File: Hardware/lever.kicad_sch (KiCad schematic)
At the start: 11 parts

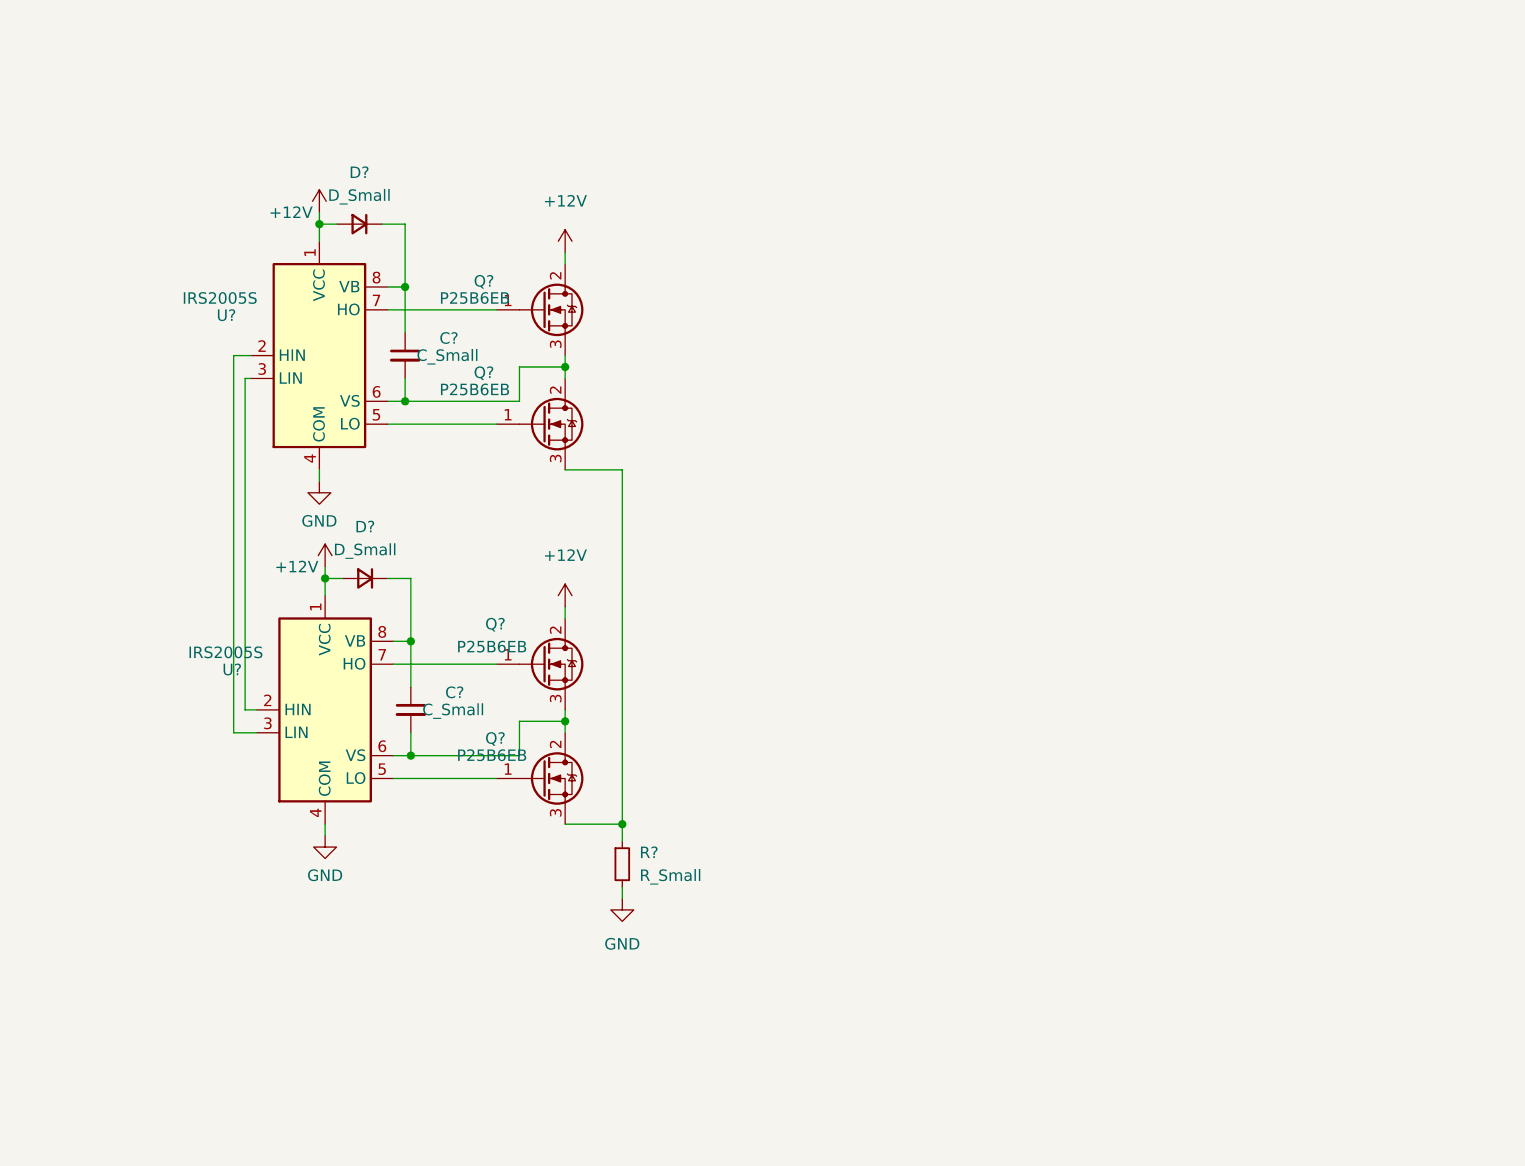
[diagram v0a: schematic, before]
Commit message: Polished coil driver. H bridge driver needs more work.
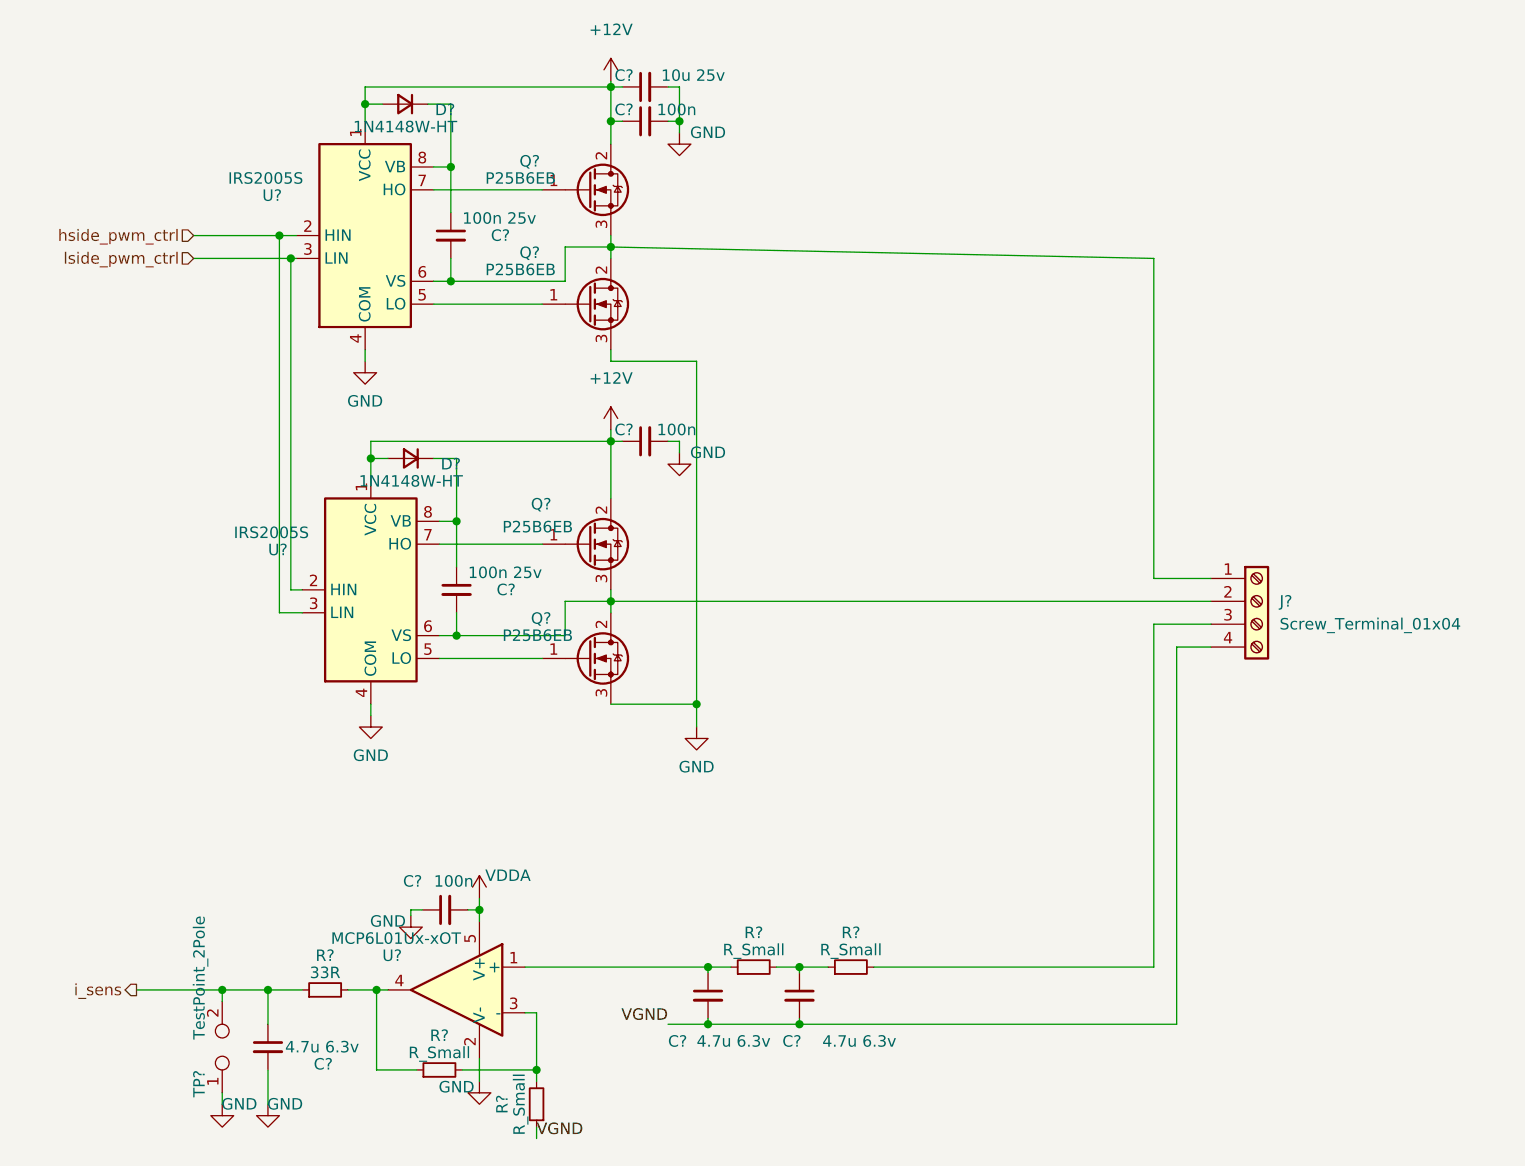
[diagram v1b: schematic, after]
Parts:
- removed C? (x2): C_Small, symbol Device:C_Small
- removed D? (x2): D_Small, symbol Device:D_Small
- removed R?: R_Small, symbol Device:R_Small
- added C? (x3): 100n, Capacitor_SMD:C_0603_1608Metric_Pad1.08x0.95mm_HandSolder, symbol Device:C_Small
- added C? (x3): 4.7u 6.3v, Capacitor_SMD:C_0603_1608Metric_Pad1.08x0.95mm_HandSolder, symbol Device:C_Small
- added C? (x2): 100n 25v, Capacitor_SMD:C_0603_1608Metric_Pad1.08x0.95mm_HandSolder, symbol Device:C_Small
- added C?: 10u 25v, Capacitor_SMD:C_0805_2012Metric_Pad1.18x1.45mm_HandSolder, symbol Device:C_Small
- added D? (x2): 1N4148W-HT, Diode_SMD:D_SOD-123, symbol Device:D_Small
- added J?: Screw_Terminal_01x04, symbol Connector:Screw_Terminal_01x04
- added R? (x4): R_Small, symbol Device:R_Small
- added R?: 33R, Resistor_SMD:R_0603_1608Metric_Pad0.98x0.95mm_HandSolder, symbol Device:R_Small
- added TP?: TestPoint_2Pole, Connector_PinHeader_2.54mm:PinHeader_1x02_P2.54mm_Vertical, symbol Connector:TestPoint_2Pole
- added U?: MCP6L01Ux-xOT, Package_TO_SOT_SMD:SOT-23-5, symbol Amplifier_Operational:MCP6L01Ux-xOT
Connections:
- net +12V: now also C?.1, C?.1, C?.1, D?.2 (A), D?.2 (A)
- net GND: now also Q?.3 (S), Q?.3 (S), C?.1, C?.2, C?.2, C?.2, C?.2, TP?.1, U?.2 (V-)
- net at U?.8 (VB): now also C?.1, D?.1 (K) (x2)
- net at Q?.2 (D), Q?.3 (S), U?.6 (VS): now also C?.2, J?.1 (Pin_1)
- net at Q?.2 (D), Q?.3 (S), U?.6 (VS): now also C?.2, J?.2 (Pin_2)
- net lside_pwm_ctrl: now reaches U?.2 (HIN), U?.3 (LIN)
- net hside_pwm_ctrl: now reaches U?.2 (HIN), U?.3 (LIN)
- new net: R?.2, R?.2, U?.3 (-)
- new net: R?.1, R?.2, U?.4
- new net: C?.1, R?.1, U?.1 (+)
- new net: C?.1, R?.1, R?.2
- new net: J?.3 (Pin_3), R?.2
- new net VDDA: C?.2, U?.5 (V+)
- new net VGND: C?.2, C?.2, J?.4 (Pin_4), R?.1
- new net i_sens: C?.1, R?.1, TP?.2
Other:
- moved on the sheet: Q?, U?

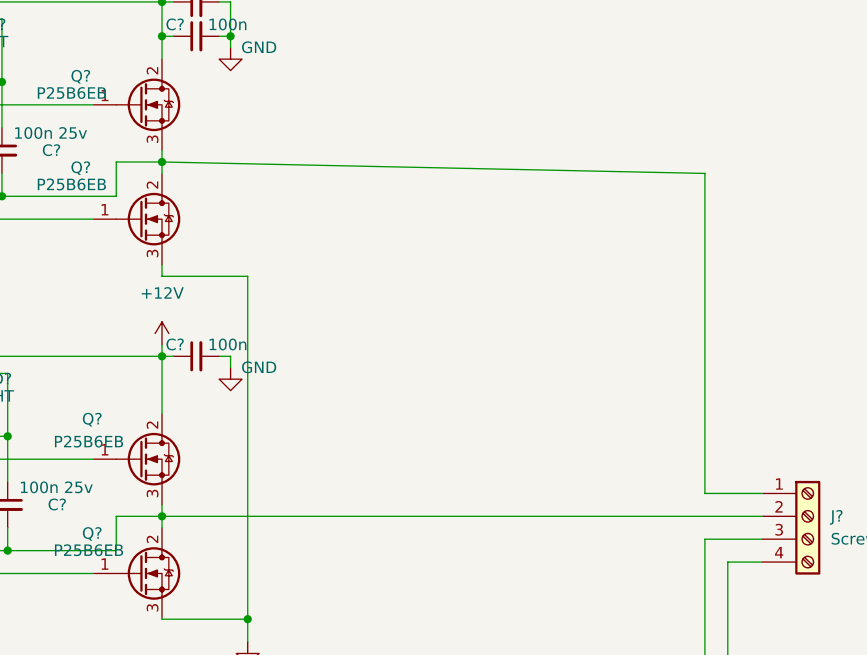
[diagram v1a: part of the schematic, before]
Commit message: Changes about piezo transducer driver
+ Regarding measurement of piezo transducer impedance, driver circuit is updated.(-+15v). Besides circuit is updated. But yet to be simulated for new resistance values.
+ Most cost efficient analog design(up to now) is created. Noise free enough, but nothing more.
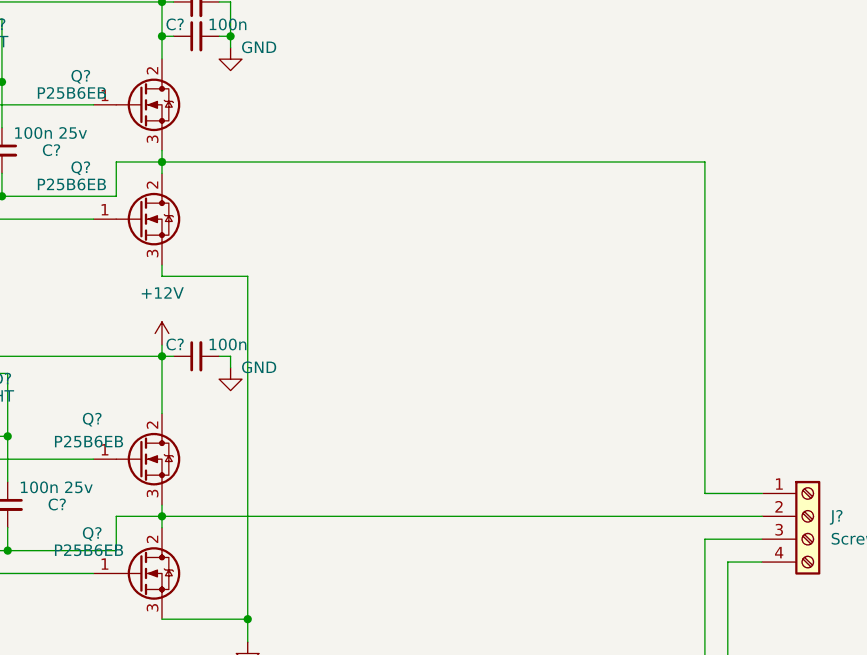
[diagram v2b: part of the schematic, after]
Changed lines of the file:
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@@
-    (stroke (width 0) (type default) (color 0 0 0 0))
-  )
-  (wire (pts (xy 206.375 62.23) (xy 206.375 97.79))
     (stroke (width 0) (type default) (color 0 0 0 0))
   )
@@
     (stroke (width 0) (type default) (color 0 0 0 0))
   )
+  (wire (pts (xy 206.375 60.96) (xy 206.375 97.79))
+    (stroke (width 0) (type default) (color 0 0 0 0))
+  )
   (wire (pts (xy 212.725 102.87) (xy 206.375 102.87))
     (stroke (width 0) (type default) (color 0 0 0 0))
@@
     (stroke (width 0) (type default) (color 0 0 0 0))
   )
-  (wire (pts (xy 146.05 60.96) (xy 206.375 62.23))
-    (stroke (width 0) (type default) (color 0 0 0 0))
-  )
   (wire (pts (xy 153.67 46.99) (xy 153.67 48.26))
     (stroke (width 0) (type default) (color 0 0 0 0))
@@
     (stroke (width 0) (type default) (color 0 0 0 0))
   )
+  (wire (pts (xy 146.05 60.96) (xy 206.375 60.96))
+    (stroke (width 0) (type default) (color 0 0 0 0))
+  )
